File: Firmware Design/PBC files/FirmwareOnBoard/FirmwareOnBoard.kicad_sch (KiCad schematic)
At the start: 20 parts, among them J1 Conn_ST_STDC14, J2 USB_C_Receptacle_USB2.0_16P, J3 Barrel_Jack_Switch, J4 NRF24L01 + PA/LNA, J5 OLED HS91L02W2C01, SW1 SW_Push, SW2 SW_Push, U1 TPS3839DBZ, U2 LM2576HVS-3.3, U3 LIS2DH, U4 SCD40-D-R1

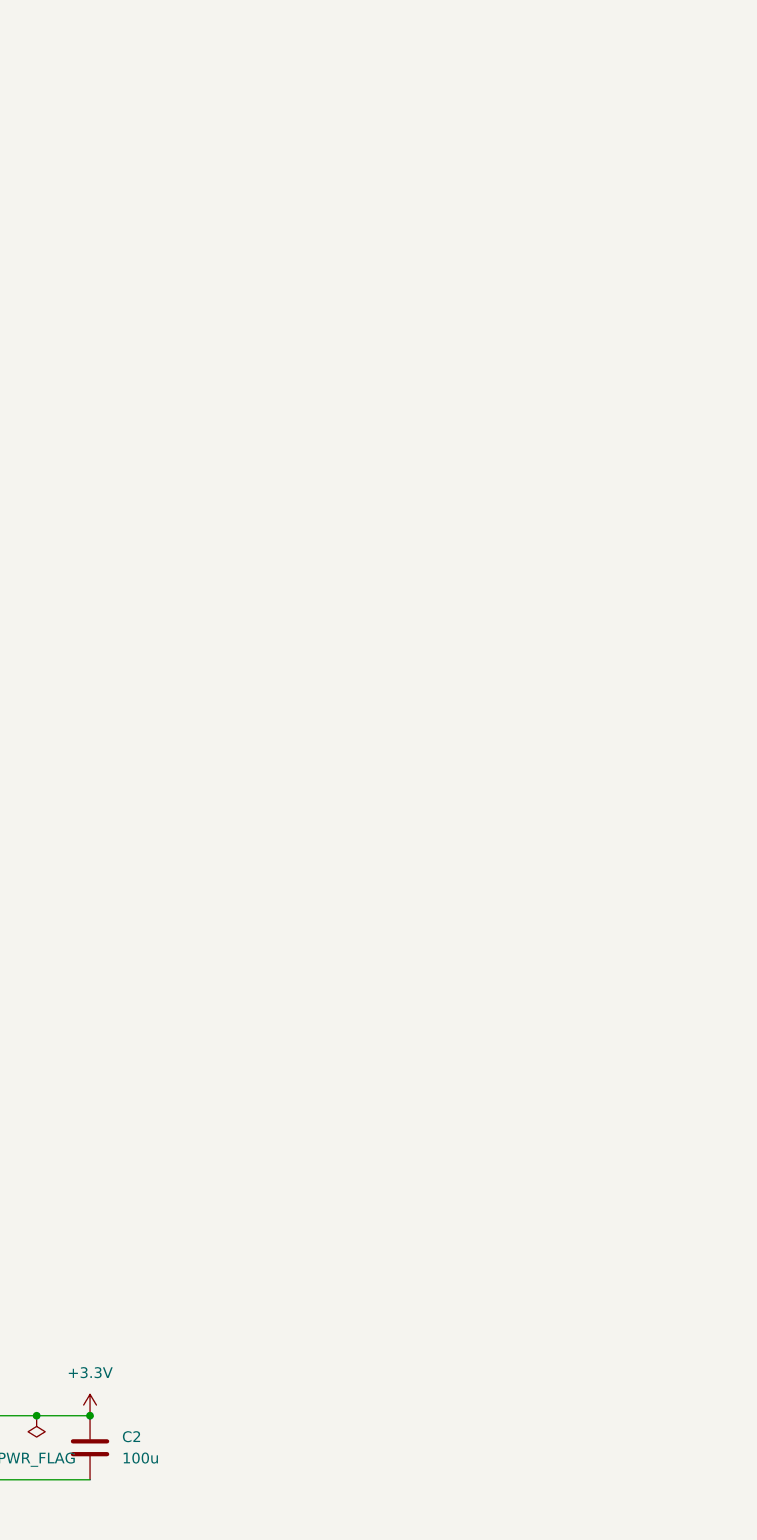
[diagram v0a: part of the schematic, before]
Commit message: Sourced MCU
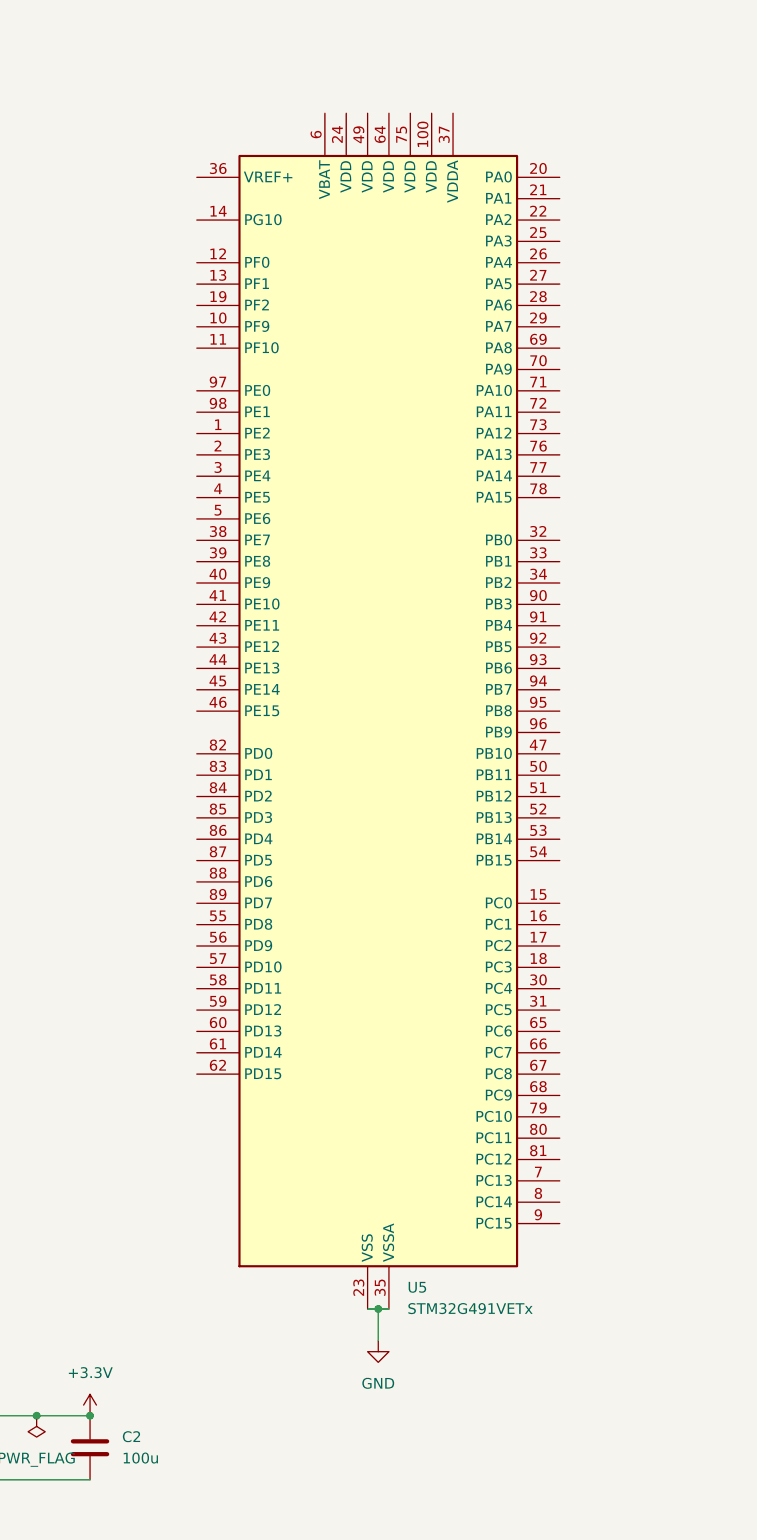
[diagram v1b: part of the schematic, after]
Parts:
- added U5: STM32G491VETx, Package_QFP:LQFP-100_14x14mm_P0.5mm, symbol MCU_ST_STM32G4:STM32G491VETx
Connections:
- net GND: now also U5.23 (VSS), U5.35 (VSSA), U5.48 (VSS), U5.63 (VSS), U5.74 (VSS), U5.99 (VSS)

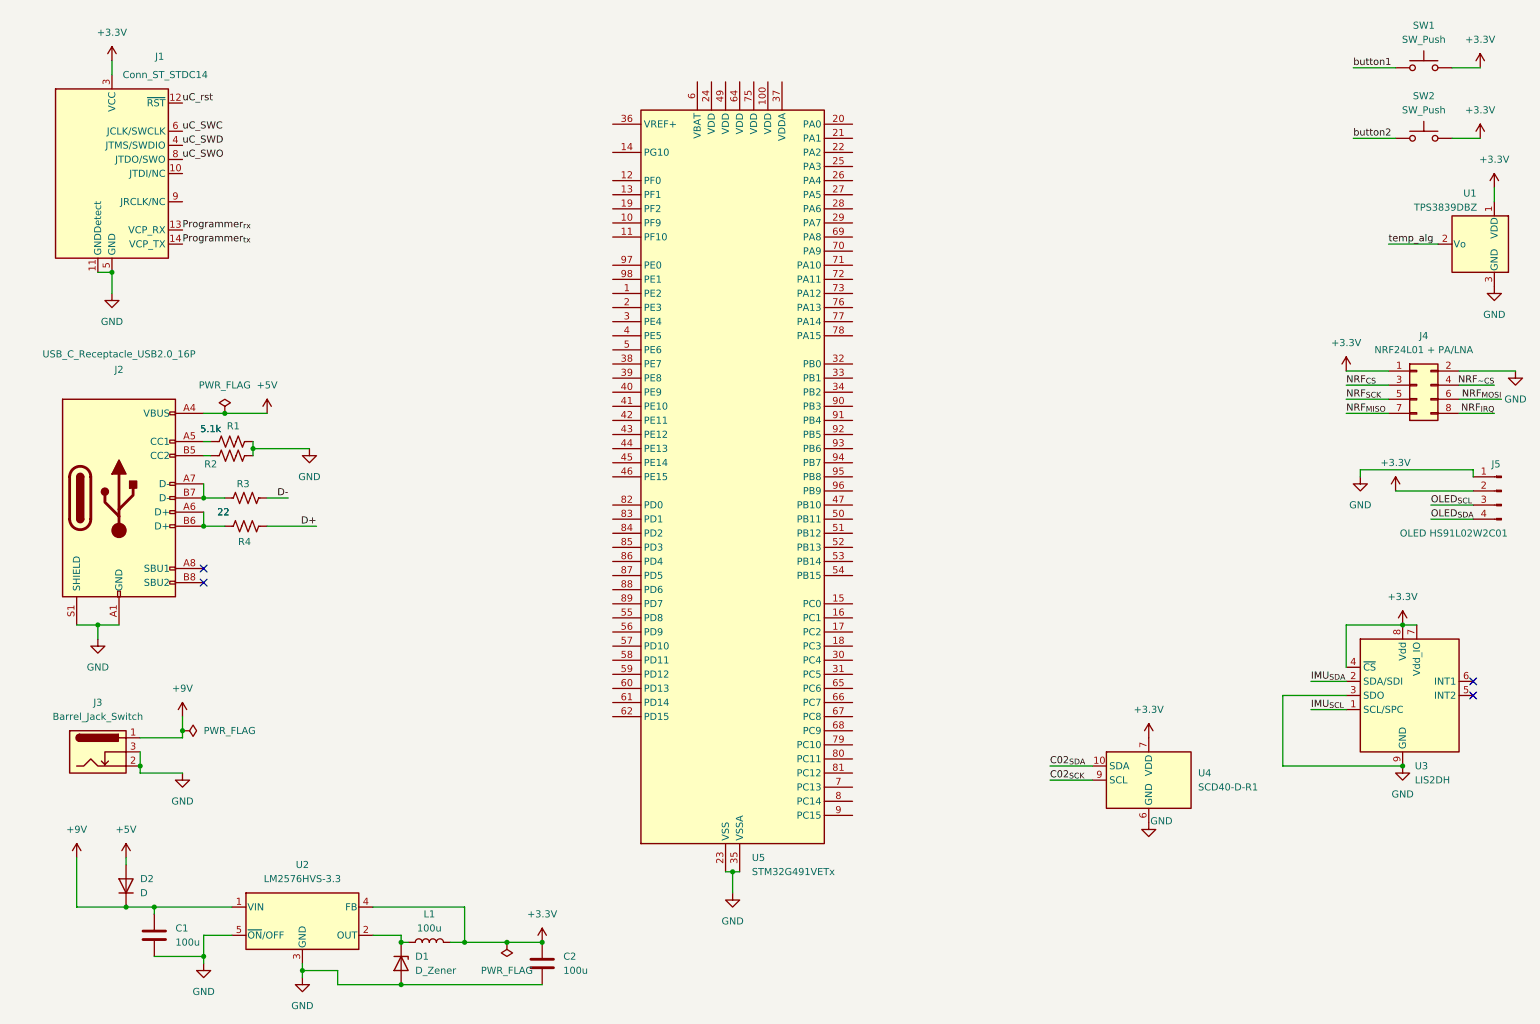
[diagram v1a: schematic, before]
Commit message: Added New MCU and many peripherals
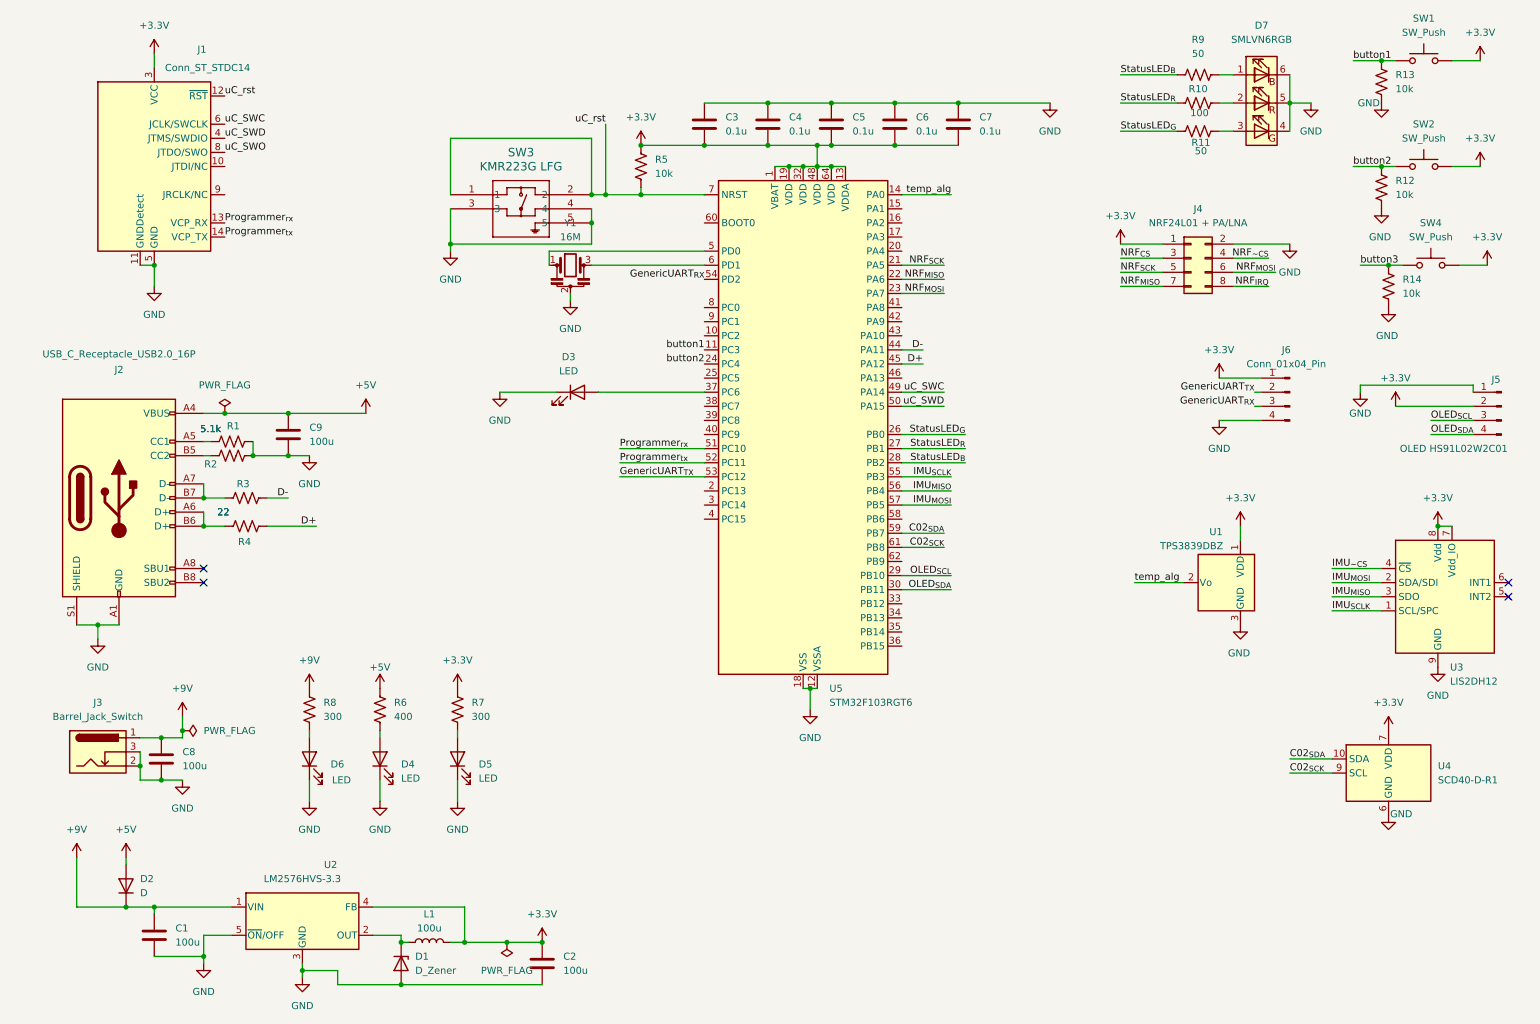
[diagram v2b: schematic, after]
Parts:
- removed U5: STM32G491VETx, Package_QFP:LQFP-100_14x14mm_P0.5mm, symbol MCU_ST_STM32G4:STM32G491VETx
- added C3, C4, C5, C6, C7: 0.1u, symbol Device:C
- added C8, C9: 100u, symbol Device:C
- added D3: LED, symbol Device:LED
- added D4, D5, D6: LED, LED_SMD:LED_0805_2012Metric, symbol Device:LED
- added D7: SMLVN6RGB, LED_SMD:LED_ROHM_SMLVN6, symbol LED:SMLVN6RGB
- added J6: Conn_01x04_Pin, symbol Connector:Conn_01x04_Pin
- added R10: 100, Resistor_SMD:R_0603_1608Metric, symbol Device:R_US
- added R11, R9: 50, Resistor_SMD:R_0603_1608Metric, symbol Device:R_US
- added R12, R13, R14, R5: 10k, symbol Device:R_US
- added R6: 400, Resistor_SMD:R_0603_1608Metric, symbol Device:R_US
- added R7, R8: 300, Resistor_SMD:R_0603_1608Metric, symbol Device:R_US
- added SW3: KMR223G LFG, flight_stick_footprints:KMR2_G_CNK, symbol flight_stick:KMR223G_LFG
- added SW4: SW_Push, symbol Switch:SW_Push
- added U5: STM32F103RGT6, Package_QFP:LQFP-64_10x10mm_P0.5mm, symbol MCU_ST_STM32F1:STM32F103RGTx
- added Y1: 16M, Crystal:Resonator_SMD_Murata_CSTxExxV-3Pin_3.0x1.1mm, symbol Device:Resonator
- U3: value LIS2DH -> LIS2DH12
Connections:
- net +3.3V: now also C3.1, C4.1, C5.1, C6.1, C7.1, J6.1 (Pin_1), R5.1, R7.1, SW4.2, U5.1 (VBAT), U5.13 (VDDA), U5.19 (VDD), U5.32 (VDD), U5.48 (VDD), U5.64 (VDD); no longer U3.4 (~{CS})
- net +5V: now also C9.1, R6.1
- net +9V: now also C8.1, R8.1
- net C02_{SCK}: now also U5.61 (PB8)
- net C02_{SDA}: now also U5.59 (PB7)
- net D+: now also U5.45 (PA12)
- net D-: now also U5.44 (PA11)
- net GND: now also C3.2, C4.2, C5.2, C6.2, C7.2, C8.2, C9.2, D3.1 (K), D4.1 (K), D5.1 (K), D6.1 (K), D7.4 (GK), D7.5 (RK), D7.6 (BK), J6.4 (Pin_4), R12.2, R13.2, R14.2, SW3.3, SW3.4, SW3.5, U5.12 (VSSA), U5.18 (VSS), U5.31 (VSS), U5.47 (VSS), U5.63 (VSS), Y1.2; no longer U3.3 (SDO)
- net NRF_{MISO}: now also U5.22 (PA6)
- net NRF_{MOSI}: now also U5.23 (PA7)
- net NRF_{SCK}: now also U5.21 (PA5)
- net OLED_{SCL}: now also U5.29 (PB10)
- net OLED_{SDA}: now also U5.30 (PB11)
- net Programmer_{rx}: now also U5.51 (PC10)
- net Programmer_{tx}: now also U5.52 (PC11)
- net button1: now also R13.1, U5.11 (PC3)
- net button2: now also R12.1, U5.24 (PC4)
- net temp_alg: now also U5.14 (PA0)
- net uC_SWC: now also U5.49 (PA14)
- net uC_SWD: now also U5.50 (PA15)
- net uC_rst: now also R5.2, SW3.1, SW3.2, U5.7 (NRST)
- net IMU_{SCL} renamed IMU_{SCLK}
- net IMU_{SCLK}: now also U5.55 (PB3)
- net IMU_{SDA} renamed IMU_{MOSI}
- net IMU_{MOSI}: now also U5.57 (PB5)
- new net: D6.2 (A), R8.2
- new net: D3.2 (A), U5.37 (PC6)
- new net: U5.5 (PD0), Y1.1
- new net: U5.6 (PD1), Y1.3
- new net: D4.2 (A), R6.2
- new net: D7.2 (RA), R10.2
- new net: D7.3 (GA), R11.2
- new net: D7.1 (BA), R9.2
- new net: D5.2 (A), R7.2
- new net GenericUART_{RX}: J6.3 (Pin_3), U5.54 (PD2)
- new net GenericUART_{TX}: J6.2 (Pin_2), U5.53 (PC12)
- new net IMU_{MISO}: U3.3 (SDO), U5.56 (PB4)
- new net IMU_{~CS}: U3.4 (~{CS})
- new net StatusLED_{B}: R9.1, U5.28 (PB2)
- new net StatusLED_{G}: R11.1, U5.26 (PB0)
- new net StatusLED_{R}: R10.1, U5.27 (PB1)
- new net button3: R14.1, SW4.1
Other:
- moved on the sheet: J1, J4, J5, SW1, SW2, U1, U3, U4

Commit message: Completed 1st draft of schematic
Filled ALL MCU pin allocations lol
2 seven seg displays (if hex, can represent 0-256)
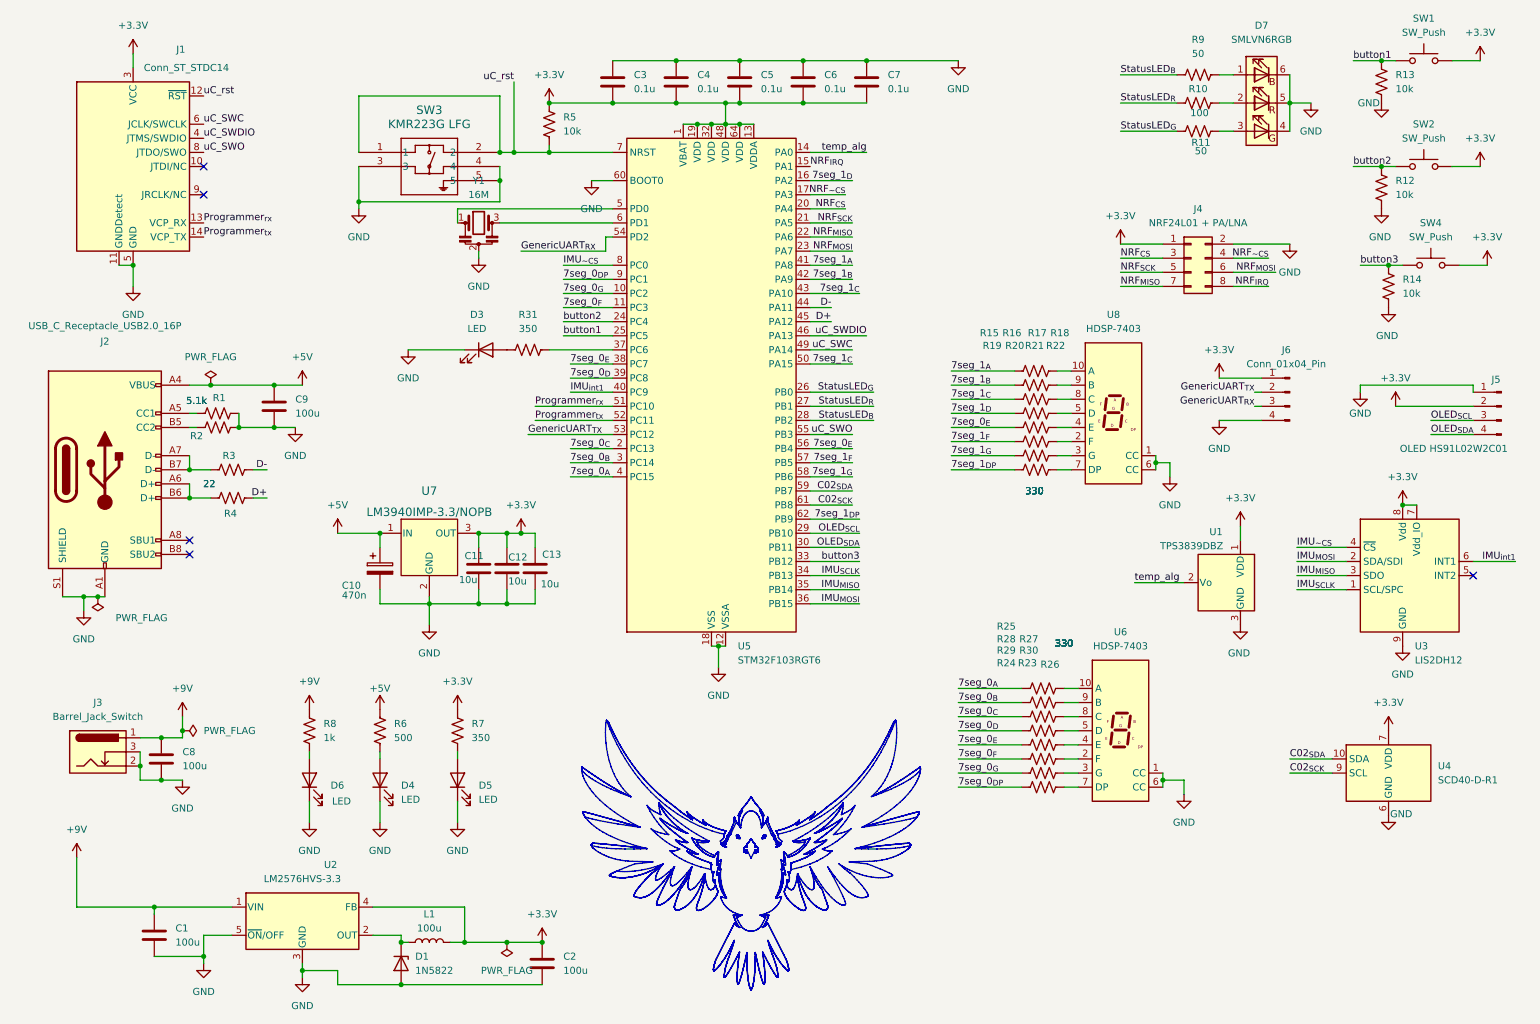
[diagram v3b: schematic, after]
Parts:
- removed D2: D, symbol Device:D
- added C10: 470n, Capacitor_SMD:C_0603_1608Metric, symbol Device:C_Polarized
- added C11, C12, C13: 10u, Capacitor_SMD:C_0603_1608Metric, symbol Device:C
- added R15, R16, R17, R18, R19, R20, R21, R22, R23, R24, R25, R26, R27, R28, R29, R30: 330, symbol Device:R_US
- added R31: 350, Resistor_SMD:R_0603_1608Metric, symbol Device:R_US
- added U6, U8: HDSP-7403, Display_7Segment:HDSP-7401, symbol Display_Character:HDSP-7403
- added U7: LM3940IMP-3.3/NOPB, flight_stick_footprints:MP04A, symbol flight_stick:LM3940IMP-3.3_NOPB
- D1: value D_Zener -> 1N5822
- R6: value 400 -> 500
- R7: value 300 -> 350
- R8: value 300 -> 1k
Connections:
- net +3.3V: now also C11.1, C12.1, C13.1, U7.3 (OUT)
- net +5V: now also C10.1, U7.1 (IN)
- net GND: now also U5.60 (BOOT0), C10.2, C11.2, C12.2, C13.2, U6.1 (CC), U6.6 (CC), U7.2 (GND), U7.4 (GND), U8.1 (CC), U8.6 (CC)
- net IMU_{MISO}: now also U5.35 (PB14); no longer U5.56 (PB4)
- net IMU_{MOSI}: now also U5.36 (PB15); no longer U5.57 (PB5)
- net IMU_{SCLK}: now also U5.34 (PB13); no longer U5.55 (PB3)
- net IMU_{~CS}: now also U5.8 (PC0)
- net NRF_{CS}: now also U5.20 (PA4)
- net NRF_{IRQ}: now also U5.15 (PA1)
- net NRF_{~CS}: now also U5.17 (PA3)
- net button1: now also U5.25 (PC5); no longer U5.11 (PC3)
- net button3: now also U5.33 (PB12)
- net uC_SWO: now also U5.55 (PB3)
- net 7seg_0_{G}: now reaches U5.10 (PC2)
- net 7seg_0_{G}: now also R29.1
- net 7seg_1_{D}: now reaches U5.16 (PA2)
- net 7seg_1_{D}: now also R18.1
- net 7seg_0_{C}: now reaches U5.2 (PC13)
- net 7seg_0_{C}: now also R25.1
- net 7seg_0_{B}: now reaches U5.3 (PC14)
- net 7seg_0_{B}: now also R24.1
- net at U5.37 (PC6): now also R31.1; no longer D3.2 (A)
- net 7seg_0_{E}: now reaches U5.38 (PC7)
- net 7seg_0_{E}: now also U5.56 (PB4), R19.1, R27.1
- net 7seg_0_{D}: now reaches U5.39 (PC8)
- net 7seg_0_{D}: now also R26.1
- net 7seg_0_{A}: now reaches U5.4 (PC15)
- net 7seg_0_{A}: now also R23.1
- net IMU_{int1}: now reaches U5.40 (PC9)
- net IMU_{int1}: now also U3.6 (INT1)
- net 7seg_1_{A}: now reaches U5.41 (PA8)
- net 7seg_1_{A}: now also R15.1
- net 7seg_1_{B}: now reaches U5.42 (PA9)
- net 7seg_1_{B}: now also R16.1
- net 7seg_1_{C}: now reaches U5.43 (PA10)
- net 7seg_1_{C}: now also U5.50 (PA15), R17.1
- net uC_SWDIO: now reaches U5.46 (PA13)
- net uC_SWDIO: now also J1.4 (JTMS/SWDIO)
- net 7seg_1_{G}: now reaches U5.58 (PB6)
- net 7seg_1_{G}: now also R21.1
- net 7seg_1_{DP}: now reaches U5.62 (PB9)
- net 7seg_1_{DP}: now also R22.1
- net 7seg_0_{DP}: now reaches U5.9 (PC1)
- net 7seg_0_{DP}: now also R30.1
- removed net uC_SWD: J1.4 (JTMS/SWDIO), U5.50 (PA15)
- new net: R28.2, U6.2 (F)
- new net: R27.2, U6.4 (E)
- new net: R21.2, U8.3 (G)
- new net: R18.2, U8.5 (D)
- new net: R24.2, U6.9 (B)
- new net: R25.2, U6.8 (C)
- new net: R15.2, U8.10 (A)
- new net: R20.2, U8.2 (F)
- new net: R19.2, U8.4 (E)
- new net: R22.2, U8.7 (DP)
- new net: R17.2, U8.8 (C)
- new net: R16.2, U8.9 (B)
- new net: R23.2, U6.10 (A)
- new net: R29.2, U6.3 (G)
- new net: R26.2, U6.5 (D)
- new net: R30.2, U6.7 (DP)
- new net: D3.2 (A), R31.2
- new net 7seg_0_{F}: R28.1, U5.11 (PC3)
- new net 7seg_1_{F}: R20.1, U5.57 (PB5)
- no-connect marks 4 -> 5
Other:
- moved on the sheet: C3, C4, C5, C6, C7, C9, D3, D4, D5, D6, J1, J2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
